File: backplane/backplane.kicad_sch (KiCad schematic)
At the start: 23 parts, among them U8 CH224K, Y6 Crystal_GND24

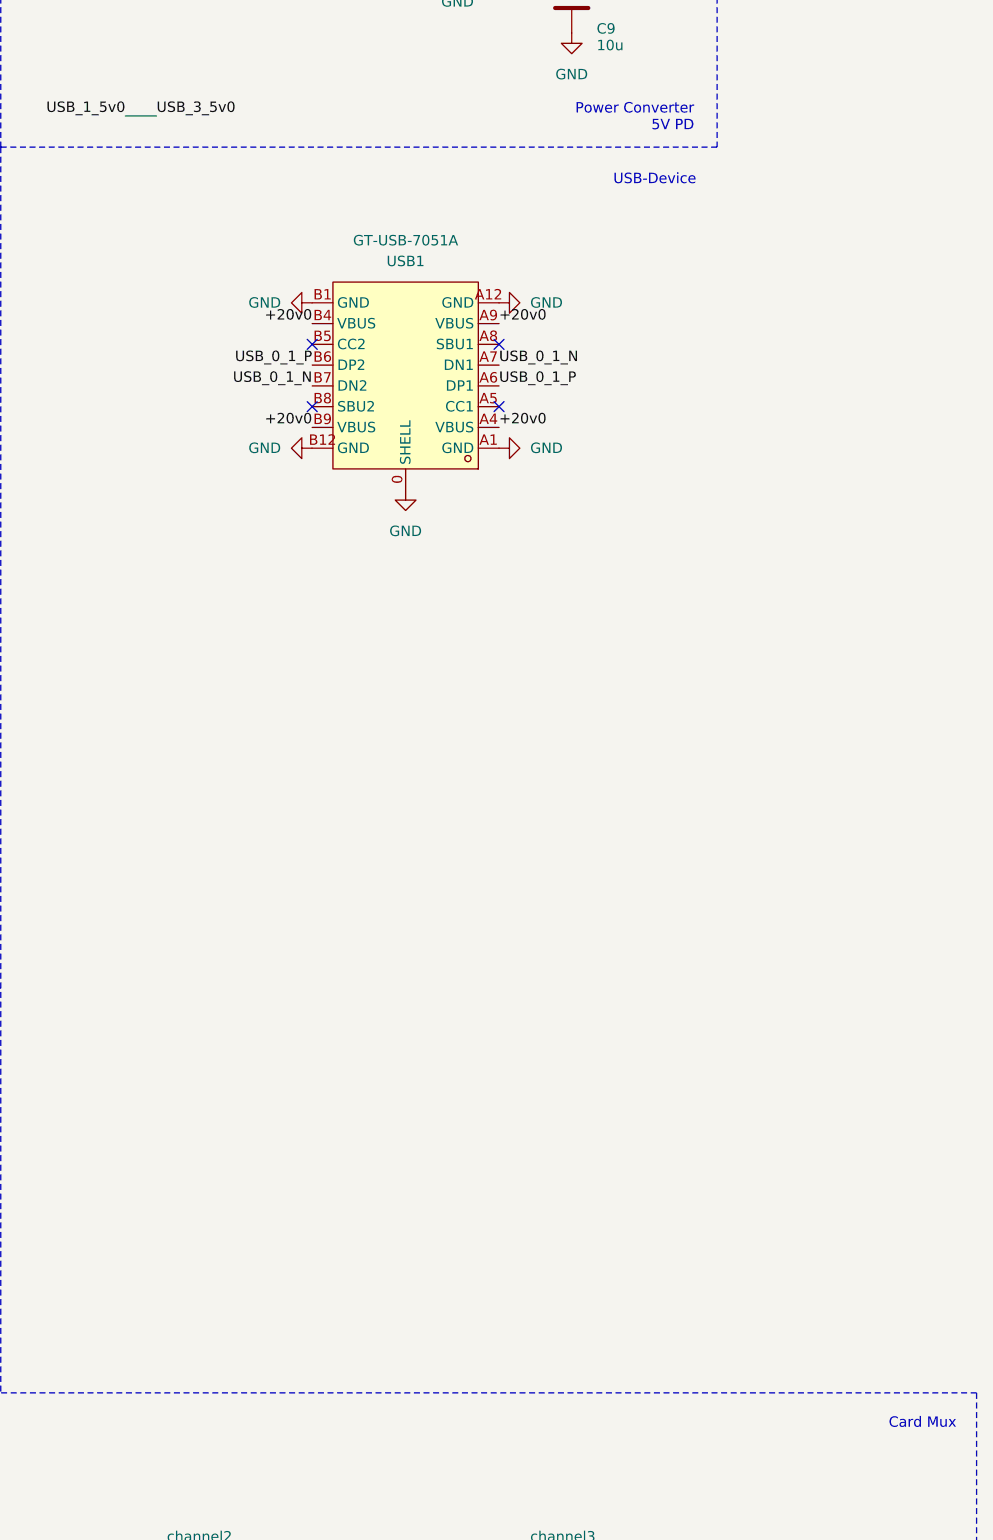
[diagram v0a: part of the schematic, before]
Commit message: Add 20V -> 3V3 buck
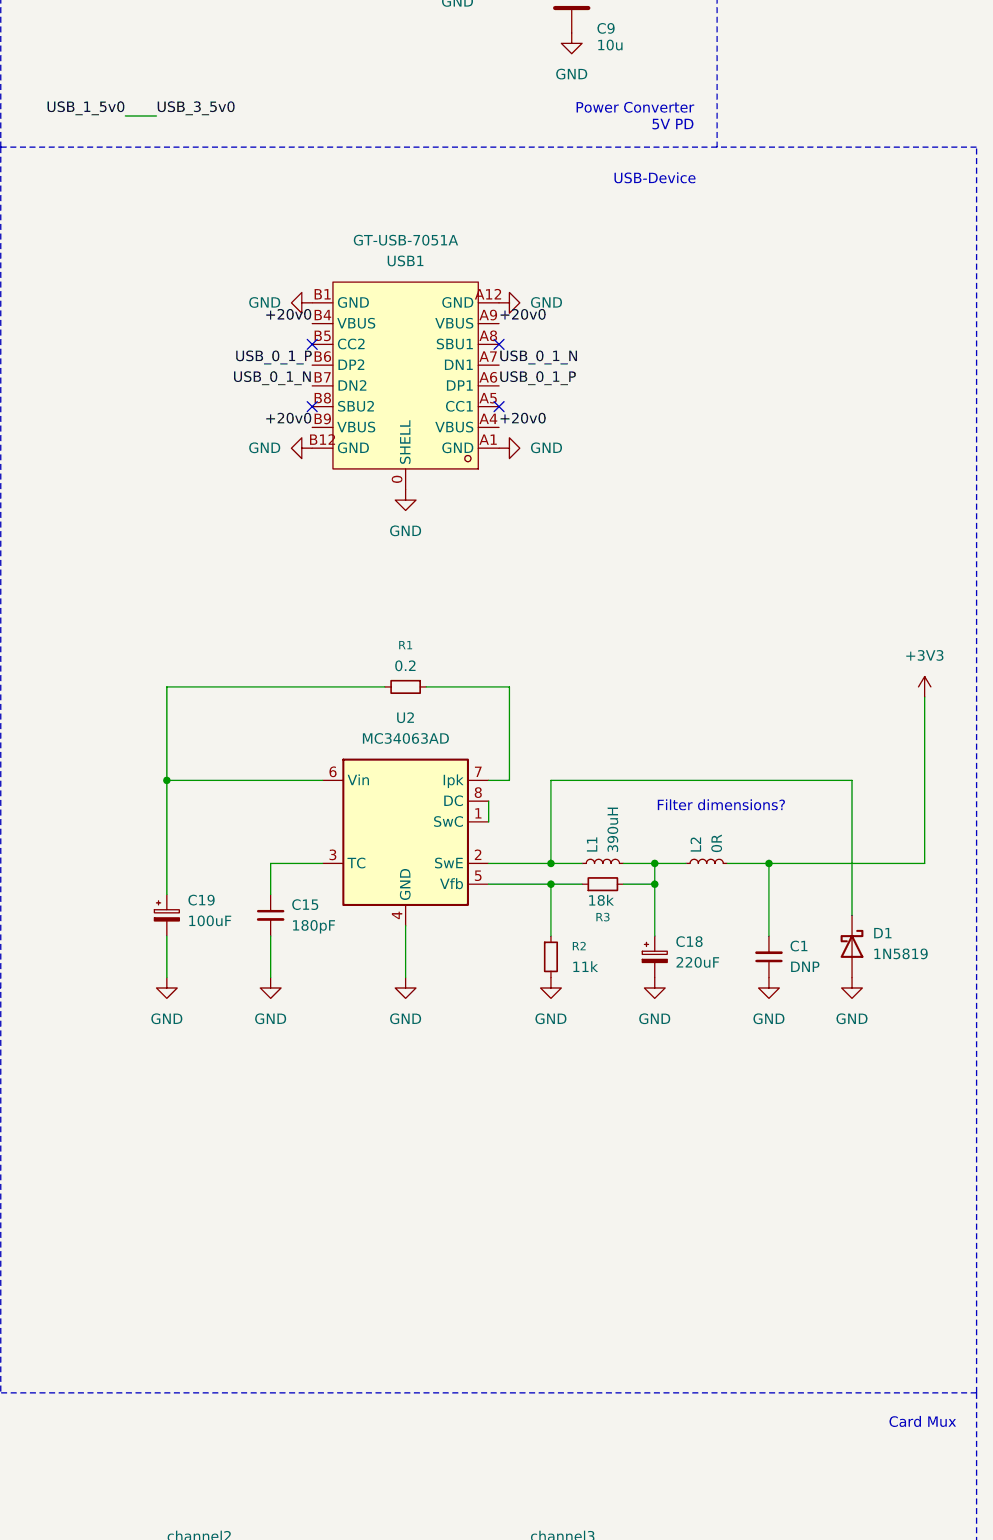
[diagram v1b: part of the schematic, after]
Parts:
- added C1: DNP, symbol Device:C_Small
- added C15: 180pF, symbol Device:C_Small
- added C18: 220uF, symbol Device:C_Polarized_Small
- added C19: 100uF, symbol Device:C_Polarized_Small
- added D1: 1N5819, Diode_THT:D_DO-41_SOD81_P10.16mm_Horizontal, symbol Diode:1N5819
- added L1: 390uH, symbol Device:L_Small
- added L2: 0R, symbol Device:L_Small
- added R1: 0.2, symbol Device:R_Small
- added R2: 11k, symbol Device:R_Small
- added R3: 18k, symbol Device:R_Small
- added U2: MC34063AD, Package_SO:SOIC-8_3.9x4.9mm_P1.27mm, symbol Regulator_Switching:MC34063AD
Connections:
- net GND: now also C1.1, C15.2, C18.2, C19.2, D1.2 (A), R2.2, U2.4 (GND)
- new net: R2.1, R3.1, U2.5 (Vfb)
- new net: C18.1, L1.2, L2.1, R3.2
- new net: D1.1 (K), L1.1, U2.2 (SwE)
- new net: R1.1, U2.7 (Ipk)
- new net: C19.1, R1.2, U2.6 (Vin)
- new net: U2.1 (SwC), U2.8 (DC)
- new net: C15.1, U2.3 (TC)
- new net +3V3: C1.2, L2.2
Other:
- note added: "Filter dimensions?"

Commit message: More work on the backplane
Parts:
- added H1, H2: MountingHole, MountingHole:MountingHole_3.2mm_M3, symbol Mechanical:MountingHole
- renumbered C13 to C1, C14 to C2, C19 to C3, C15 to C4, C9 to C5, C18 to C6, C1 to C7, D27 to D1, D28 to D2, D29 to D3, D30 to D4, D31 to D5, D21 to D6, D1 to D7, R22 to R1, R2 to R10, R14 to R11, R3 to R12, R23 to R2, R24 to R3, R18 to R4, R15 to R5, R16 to R6, R17 to R7, R1 to R8, R13 to R9, U11 to U1, U8 to U2, U2 to U3, USB3 to USB1, USB1 to USB2, Y6 to Y1
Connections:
- net USB_2_3v3 is gone; now on net USB_3v3: C1.1, D5.2 (A)
- net XIN_2 is gone; now on net XIN: Y1.1
- net XOUT_2 is gone; now on net XOUT: Y1.3
- net +20v0: now also C3.1, R8.2, U3.6 (Vin)
- net USB_1_5v0: no longer U1.19 (V5)
- net +3V3 renamed +3v3
- net PLED1_1 renamed PLED1
- net PLED2_1 renamed PLED2
- net PLED4_1 renamed PLED4
- net USB_0_1_N renamed USB_N
- net USB_0_1_P renamed USB_P
- net USB_1_1_N renamed USB_3N
- net USB_1_1_P renamed USB_3P
- net USB_1_2_N renamed USB_4N
- net USB_1_2_P renamed USB_4P
- net USB_1_3_N renamed USB_2N
- net USB_1_3_P renamed USB_2P
- net USB_1_3v3 renamed USB_3v3
- net USB_1_4_N renamed USB_1N
- net USB_1_4_P renamed USB_1P
- net USB_2_5v0 renamed USB_5v
- net USB_5v: now also U1.19 (V5)
- net XIN_1 renamed XIN
- net XOUT_1 renamed XOUT
- no-connect marks 10 -> 12
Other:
- removed sheet channel3
